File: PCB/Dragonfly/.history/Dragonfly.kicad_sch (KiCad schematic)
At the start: 235 parts, among them J1 Conn_01x04_Pin, J2 Micro_SD_Card, J3 Conn_01x02_Pin, J4 Conn_01x02_Pin, J5 Conn_01x02_Pin, J6 Conn_01x02_Pin, J7 Conn_01x02, J8 CAM VIN, J9 VOUT, Q1 Q_NMOS_GDS, Q10 Q_NMOS_GDS, Q11 Q_NMOS_GDS, Q12 Q_NMOS_GDS, Q13 Q_NMOS_GDS, Q14 Q_NMOS_GDS, Q15 Q_NMOS_GDS, Q16 Q_NMOS_GDS, Q17 Q_NMOS_GDS, Q18 Q_NMOS_GDS, Q19 Q_NMOS_GDS, Q2 Q_NMOS_GDS, Q20 Q_NMOS_GDS, Q21 Q_NMOS_GDS, Q22 Q_NMOS_GDS, Q23 Q_NMOS_GDS, Q24 Q_NMOS_GDS, Q3 Q_NMOS_GDS, Q4 Q_NMOS_GDS, Q5 Q_NMOS_GDS, Q6 Q_NMOS_GDS, Q7 Q_NMOS_GDS, Q8 Q_NMOS_GDS, Q9 Q_NMOS_GDS, SW1 SW_SPST, SW2 SW_SPST, U1 STM32F405RGTx, U10 FD6288Q, U11 TPS5430DDA, U12 AMS1117-3.3, U13 L78L08_SO8, U14 AT7456E, U15 BMP280, U2 ICM-20602, U3 AT32F421G8U7, U4 FD6288Q, U5 AT32F421G8U7, U6 FD6288Q, U7 AT32F421G8U7, U8 FD6288Q, U9 AT32F421G8U7, X1 TSX-3225, Y1 27MHZ

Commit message: Update Dragonfly.kicad_sch
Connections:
- net ESC2_l011 is gone; now on net ESC2_L011: R24.2
- net ESC2_l012 is gone; now on net ESC2_L012: R38.2
- net ESC2_l013 is gone; now on net ESC2_L013: R58.2
- net ESC2_l014 is gone; now on net ESC2_L014: R78.2
- net ESC2_l021 is gone; now on net ESC2_L021: R21.2
- net ESC2_l022 is gone; now on net ESC2_L022: R40.2
- net ESC2_l023 is gone; now on net ESC2_L023: R60.2
- net ESC2_l024 is gone; now on net ESC2_L024: R80.2
- net SWCLK3: no longer J6.1 (Pin_1)
- net SWCLK4: now also J6.1 (Pin_1)
- net SWDIO3: no longer J6.2 (Pin_2)
- net SWDIO4: now also J6.2 (Pin_2)
- no-connect marks 70 -> 67
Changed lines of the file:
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@@
 	)
 	(junction
-		(at 302.26 254)
-		(diameter 0)
-		(color 0 0 0 0)
-	)
-	(junction
 		(at 391.16 71.12)
 		(diameter 0)
@@
 	)
 	(junction
+		(at 302.26 254)
+		(diameter 0)
+		(color 0 0 0 0)
+	)
+	(junction
 		(at 467.36 445.77)
 		(diameter 0)
@@
 	)
 	(no_connect
-		(at 514.35 513.08)
-	)
-	(no_connect
 		(at 147.32 317.5)
 	)
@@
 	)
 	(no_connect
-		(at 156.21 510.54)
-	)
-	(no_connect
 		(at 147.32 520.7)
 	)
@@
 	)
 	(no_connect
-		(at 514.35 307.34)
-	)
-	(no_connect
 		(at 160.02 300.99)
 	)
@@
 	(wire
 		(pts
-			(xy 302.26 250.19) (xy 342.9 250.19)
+			(xy 302.26 250.19) (xy 323.85 250.19)
 		)
 		(stroke
@@
 		)
 	)
-	(global_label "ESC2_l013"
+	(global_label "ESC2_L013"
 		(shape input)
 		(at 307.34 474.98 180)
@@
 		)
 		(property "Intersheetrefs" "${INTERSHEET_REFS}"
-			(at 294.2555 474.98 0)
+			(at 293.8926 474.98 0)
 			(hide yes)
 			(show_name no)
@@
 		)
 	)
-	(global_label "ESC2_l023"
+	(global_label "ESC2_L023"
 		(shape input)
 		(at 312.42 519.43 180)
@@
 		)
 		(property "Intersheetrefs" "${INTERSHEET_REFS}"
-			(at 299.3355 519.43 0)
+			(at 298.9726 519.43 0)
 			(hide yes)
 			(show_name no)
@@
 		)
 	)
-	(global_label "ESC2_l021"
+	(global_label "ESC2_L021"
 		(shape input)
 		(at 312.42 316.23 180)
@@
 		)
 		(property "Intersheetrefs" "${INTERSHEET_REFS}"
-			(at 299.3355 316.23 0)
+			(at 298.9726 316.23 0)
 			(hide yes)
 			(show_name no)
@@
 		)
 	)
-	(global_label "ESC2_l014"
+	(global_label "ESC2_L014"
 		(shape input)
 		(at 665.48 477.52 180)
@@
 		)
 		(property "Intersheetrefs" "${INTERSHEET_REFS}"
-			(at 652.3955 477.52 0)
+			(at 652.0326 477.52 0)
 			(hide yes)
 			(show_name no)
@@
 		)
 	)
-	(global_label "SWCLK3"
+	(global_label "SWCLK4"
 		(shape input)
 		(at 433.07 577.85 0)
@@
 		)
 	)
-	(global_label "ESC2_l012"
+	(global_label "ESC2_L012"
 		(shape input)
 		(at 665.48 271.78 180)
@@
 		)
 		(property "Intersheetrefs" "${INTERSHEET_REFS}"
-			(at 652.3955 271.78 0)
+			(at 652.0326 271.78 0)
 			(hide yes)
 			(show_name no)
@@
 		)
 	)
-	(global_label "ESC2_l022"
+	(global_label "ESC2_L022"
 		(shape input)
 		(at 670.56 316.23 180)
@@
 		)
 		(property "Intersheetrefs" "${INTERSHEET_REFS}"
-			(at 657.4755 316.23 0)
+			(at 657.1126 316.23 0)
 			(hide yes)
 			(show_name no)
@@
 		)
 	)
-	(global_label "ESC2_l024"
+	(global_label "ESC2_L024"
 		(shape input)
 		(at 670.56 521.97 180)
@@
 		)
 		(property "Intersheetrefs" "${INTERSHEET_REFS}"
-			(at 657.4755 521.97 0)
+			(at 657.1126 521.97 0)
 			(hide yes)
 			(show_name no)
@@
 		)
 	)
-	(global_label "ESC2_l011"
+	(global_label "ESC2_L011"
 		(shape input)
 		(at 307.34 271.78 180)
@@
 		)
 		(property "Intersheetrefs" "${INTERSHEET_REFS}"
-			(at 294.2555 271.78 0)
+			(at 293.8926 271.78 0)
 			(hide yes)
 			(show_name no)
@@
 		)
 	)
-	(global_label "SWDIO3"
+	(global_label "SWDIO4"
 		(shape input)
 		(at 433.07 580.39 0)
@@
 		)
 		(property "Value" "10k"
-			(at 327.152 549.148 90)
+			(at 326.898 548.386 90)
 			(show_name no)
 			(do_not_autoplace no)

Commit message: Update Dragonfly.kicad_sch
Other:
- moved on the sheet: C15, C16, C17, C18, C19, C20, J2, R6, U2

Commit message: Update Dragonfly.kicad_sch
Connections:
- net ESC2 C1 is gone; now on net ESC2_C1: C24.2, Q1.2 (D), Q2.3 (S), U4.12 (VS3)
- net ESC2 C2 is gone; now on net ESC2_C2: C37.2, Q10.3 (S), Q9.2 (D), U6.12 (VS3)
- net ESC2 C3 is gone; now on net ESC2_C3: C46.2, Q15.2 (D), Q16.3 (S), U8.12 (VS3)
- net ESC2 C4 is gone; now on net ESC2_C4: C55.2, Q21.2 (D), Q22.3 (S), U10.12 (VS3)
- net 5V: now also C62.1, C63.1, U12.3 (VI)
- net HI12: no longer U10.22 (HIN1)
- net HI14: now also U10.22 (HIN1)
- net HI22: no longer U10.23 (HIN2)
- net HI24: now also U10.23 (HIN2)
- net HI32: no longer U10.24 (HIN3)
- net HI34: now also U10.24 (HIN3)
- net LI12: no longer U10.1 (LIN1)
- net LI14: now also U10.1 (LIN1)
- net LI22: no longer U10.2 (LIN2)
- net LI24: now also U10.2 (LIN2)
- net LI32: no longer U10.3 (LIN3)
- net LI34: now also U10.3 (LIN3)
- net VOUT: no longer C62.1, C63.1, U12.3 (VI)
- net PA13 renamed SWDIO
- net PA14 renamed SWCLK
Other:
- moved on the sheet: +10ppm1, C1, C10, C11, C12, C13, C14, C15, C16, C17, C18, C19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

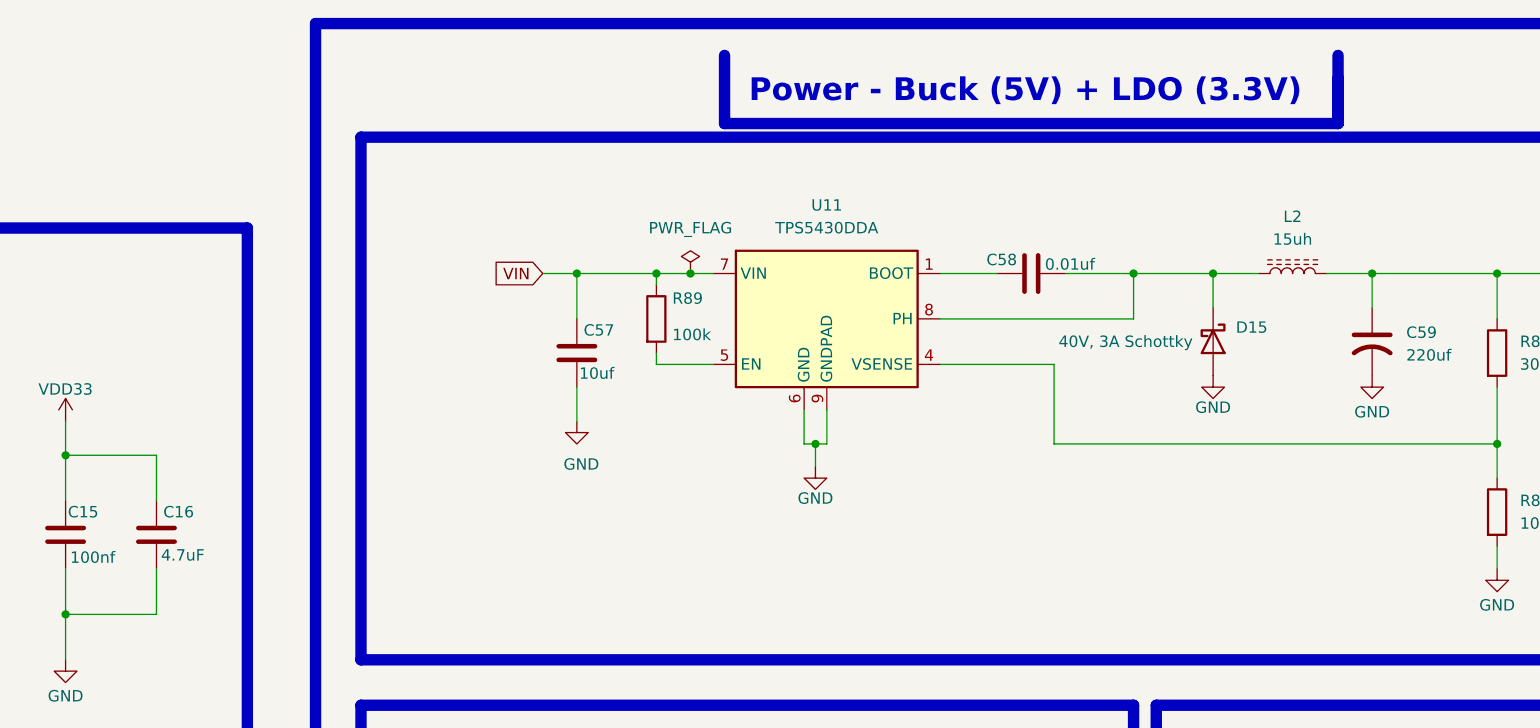
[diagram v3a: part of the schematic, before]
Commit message: Update Dragonfly.kicad_sch
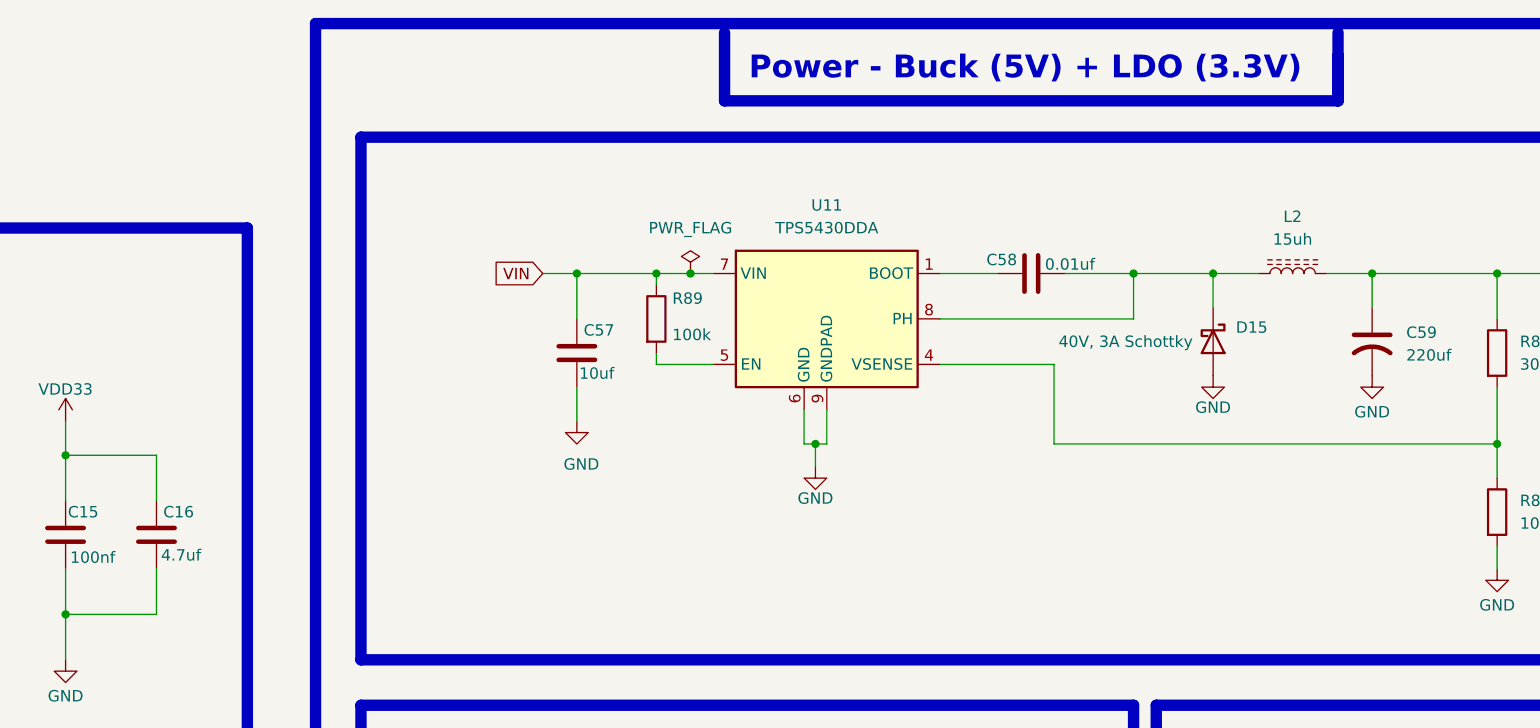
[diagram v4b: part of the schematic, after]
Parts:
- C16: value 4.7uF -> 4.7uf
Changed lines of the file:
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@@
 	(text " Power - Buck (5V) + LDO (3.3V)"
 		(exclude_from_sim no)
-		(at 518.16 27.94 0)
+		(at 518.16 25.4 0)
 		(effects
 			(font
@@
 	(polyline
 		(pts
-			(xy 553.72 26.416) (xy 553.72 31.496)
+			(xy 553.72 23.876) (xy 553.72 28.956)
 		)
 		(stroke
@@
 	(polyline
 		(pts
-			(xy 485.14 23.876) (xy 485.14 31.496)
+			(xy 485.14 21.336) (xy 485.14 28.956)
 		)
 		(stroke
@@
 	(polyline
 		(pts
-			(xy 553.72 31.496) (xy 553.72 23.876)
+			(xy 553.72 28.956) (xy 553.72 21.336)
 		)
 		(stroke
@@
 	(polyline
 		(pts
-			(xy 485.14 31.496) (xy 553.72 31.496)
+			(xy 485.14 28.956) (xy 553.72 28.956)
 		)
 		(stroke
@@
 			)
 		)
-		(property "Value" "4.7uF"
+		(property "Value" "4.7uf"
 			(at 422.148 79.756 0)
 			(show_name no)

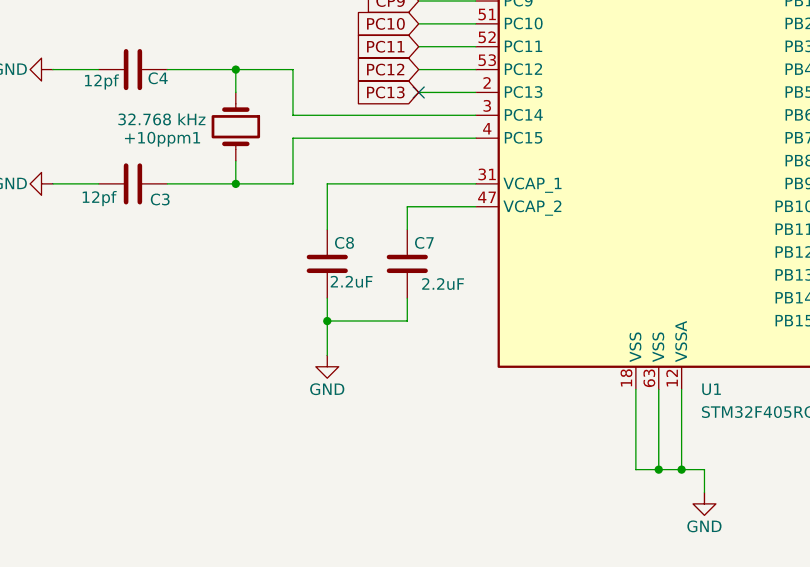
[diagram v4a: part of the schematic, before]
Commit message: Update Dragonfly.kicad_sch
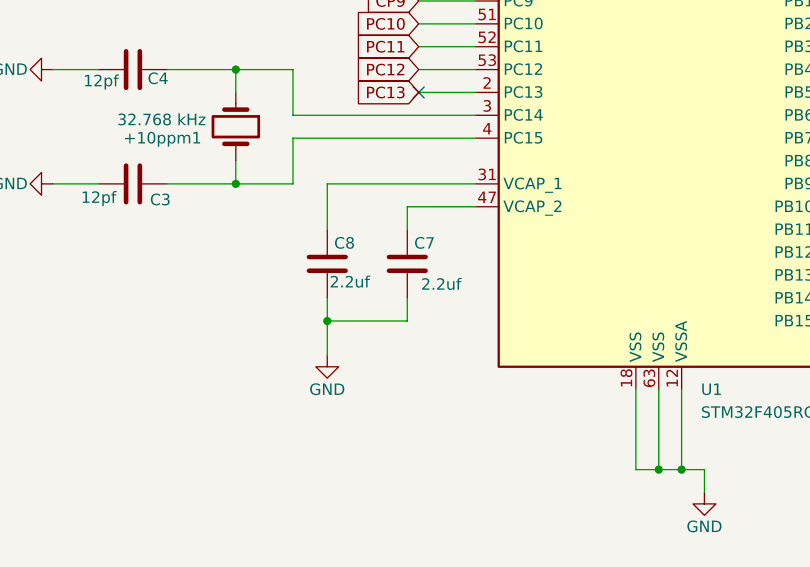
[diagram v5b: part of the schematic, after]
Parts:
- C7, C8: value 2.2uF -> 2.2uf
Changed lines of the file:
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@@
 			)
 		)
-		(property "Value" "2.2uF"
+		(property "Value" "2.2uf"
 			(at 110.744 151.892 0)
 			(show_name no)
@@
 			)
 		)
-		(property "Value" "2.2uF"
+		(property "Value" "2.2uf"
 			(at 120.904 152.146 0)
 			(show_name no)

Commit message: updated
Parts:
- removed D16: 40V, 3A Schottky, symbol Device:D_Schottky
- removed J7: Conn_01x02, symbol Connector_Generic:Conn_01x02
- added J7: XT60PW-M, XT60PW-M:AMASS_XT60PW-M, symbol XT60PW-M:XT60PW-M
- +10ppm1, Y1: footprint (none) -> Crystal:Crystal_SMD_3225-4Pin_3.2x2.5mm
- C1, C10, C11, C12, C13, C14, C15, C16, C17, C18, C19, C2, C20, C21, C22, C23, C24, C25, C26, C27, C28, C29, C3, C30, C31, C32, C33, C34, C35, C36, C37, C38, C39, C4, C40, C41, C42, C43, C44, C45, C46, C47, C48, C49, C5, C50, C51, C52, C53, C54, C55, C56, C57, C58, C6, C60, C61, C62, C63, C64, C65, C66, C67, C68, C69, C7, C70, C71, C72, C73, C8, C9: footprint (none) -> Capacitor_SMD:C_0402_1005Metric
- C59: footprint (none) -> Capacitor_SMD:CP_Elec_6.3x5.8
- D1, D2: footprint (none) -> LED_SMD:LED_0201_0603Metric
- J1: footprint (none) -> Connector_JST:JST_EH_B4B-EH-A_1x04_P2.50mm_Vertical
- J2: footprint (none) -> Connector_Card:microSD_HC_Molex_104031-0811
- J3, J4, J5, J6, J8, J9: footprint (none) -> Connector_JST:JST_EH_S2B-EH_1x02_P2.50mm_Horizontal
- L1: footprint (none) -> Inductor_SMD:L_0402_1005Metric
- L2: footprint (none) -> Inductor_SMD_Wurth:L_Wurth_WE-LQSH-4020
- R1, R10, R11, R12, R13, R14, R15, R16, R17, R18, R19, R2, R20, R21, R22, R23, R24, R25, R26, R27, R28, R29, R3, R30, R31, R32, R33, R34, R35, R36, R37, R38, R39, R4, R40, R41, R42, R43, R44, R45, R46, R47, R48, R49, R5, R50, R51, R52, R53, R54, R55, R56, R57, R58, R59, R6, R60, R61, R62, R63, R64, R65, R66, R67, R68, R69, R7, R70, R71, R72, R73, R74, R75, R76, R77, R78, R79, R8, R80, R81, R82, R83, R84, R85, R86, R88, R89, R9: footprint (none) -> Resistor_SMD:R_0402_1005Metric
- R87: footprint (none) -> Resistor_SMD:R_0815_2038Metric
- R90, R91: value 75 Ω -> 75R; footprint (none) -> Resistor_SMD:R_0402_1005Metric
- SW1, SW2: footprint (none) -> Button_Switch_SMD:SW_SPST_EVQP7A
- U10, U4, U6, U8: footprint QFN50P400X400X90-25N -> FD6288Q:QFN50P400X400X90-25N
- U14: footprint SOP65P637X110-28N -> AT7456E:SOP65P640X120-29N
- U3, U5, U7, U9: footprint AT32F421G8U7:AT32F421G8U7 -> Library:AT32F421G8U7
- X1: footprint TSX-3225 -> TSX-3225:TSX-3225
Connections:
- net GND: now also J7.2 (N), J7.SH1 (SHIELD), J7.SH2 (SHIELD)
- net VIN: now also J7.1 (P)
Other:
- moved on the sheet: J1

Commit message: Update Dragonfly.kicad_sch
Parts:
- J3, J4, J5, J6, J8, J9: footprint Connector_JST:JST_EH_S2B-EH_1x02_P2.50mm_Horizontal -> Connector_JST:JST_EH_B2B-EH-A_1x02_P2.50mm_Vertical
- Q1, Q10, Q11, Q12, Q13, Q14, Q15, Q16, Q17, Q18, Q19, Q2, Q20, Q21, Q22, Q23, Q24, Q3, Q4, Q5, Q6, Q7, Q8, Q9: footprint (none) -> Package_SON:Diodes_PowerDI3333-8
- SW1, SW2: footprint Button_Switch_SMD:SW_SPST_EVQP7A -> Button_Switch_SMD:SW_Tactile_SPST_NO_Straight_CK_PTS636Sx25SMTRLFS
- U3, U5, U7, U9: footprint Library:AT32F421G8U7 -> Package_DFN_QFN:QFN-28_4x4mm_P0.5mm
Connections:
- net VDD33: no longer C14.1, L1.2
- new net: C14.1, L1.2
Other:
- moved on the sheet: C72, C73, U15

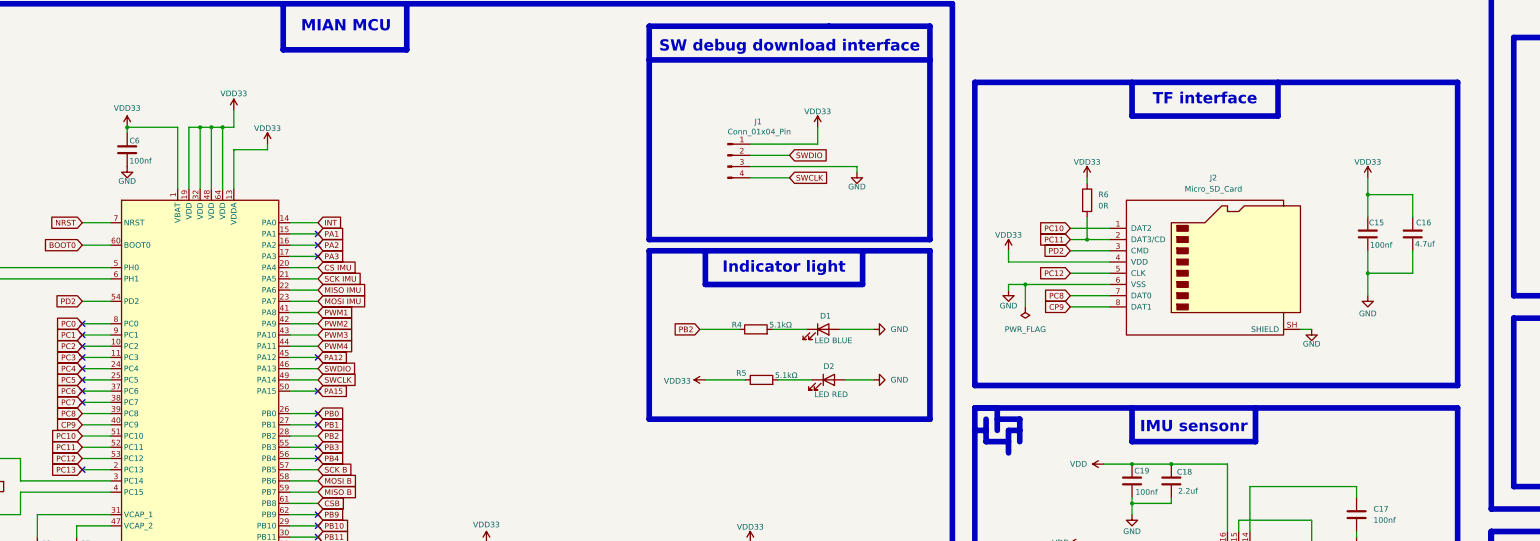
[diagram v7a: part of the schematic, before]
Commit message: Update Dragonfly.kicad_sch
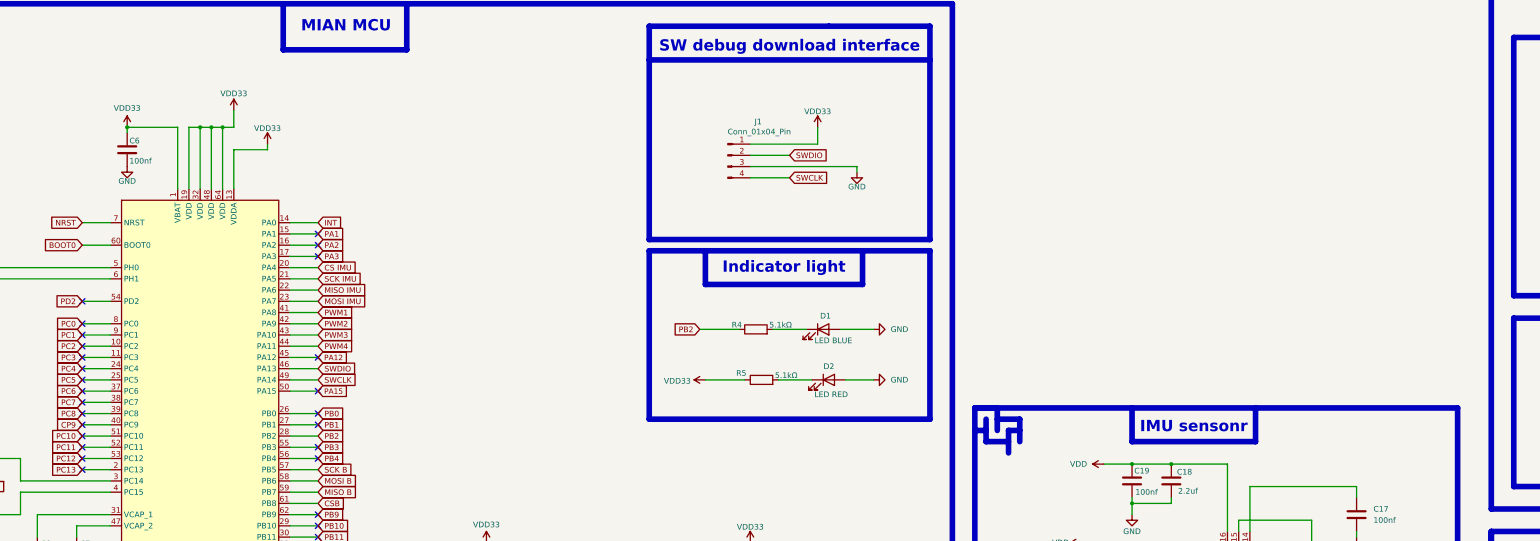
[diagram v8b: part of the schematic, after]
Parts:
- removed C15: 100nf, Capacitor_SMD:C_0402_1005Metric, symbol Device:C
- removed C16: 4.7uf, Capacitor_SMD:C_0402_1005Metric, symbol Device:C
- removed J2: Micro_SD_Card, Connector_Card:microSD_HC_Molex_104031-0811, symbol Connector:Micro_SD_Card
- removed R6: 0R, Resistor_SMD:R_0402_1005Metric, symbol Device:R
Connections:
- no-connect marks 67 -> 73
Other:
- note removed: "TF interface"
